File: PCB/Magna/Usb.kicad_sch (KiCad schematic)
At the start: 13 parts, among them J801 USB_A, J802 USB_C_Receptacle_USB2.0, U702 USB3300-EZK

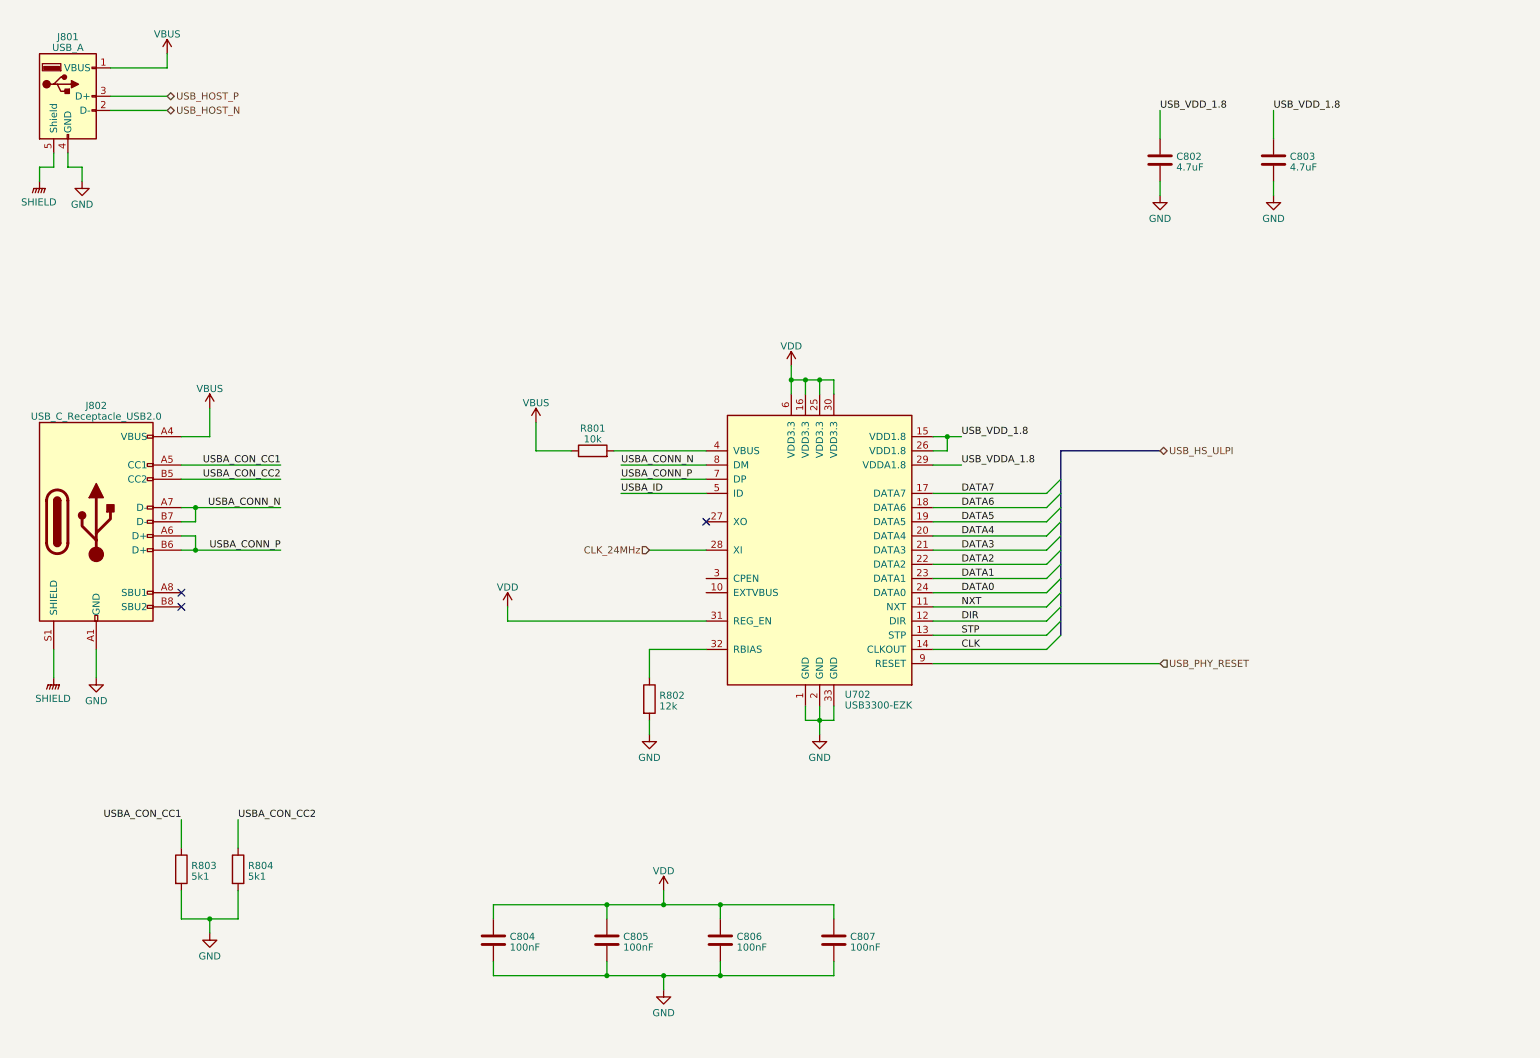
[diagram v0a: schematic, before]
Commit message: Update analogue frontend and add potentiometer interface
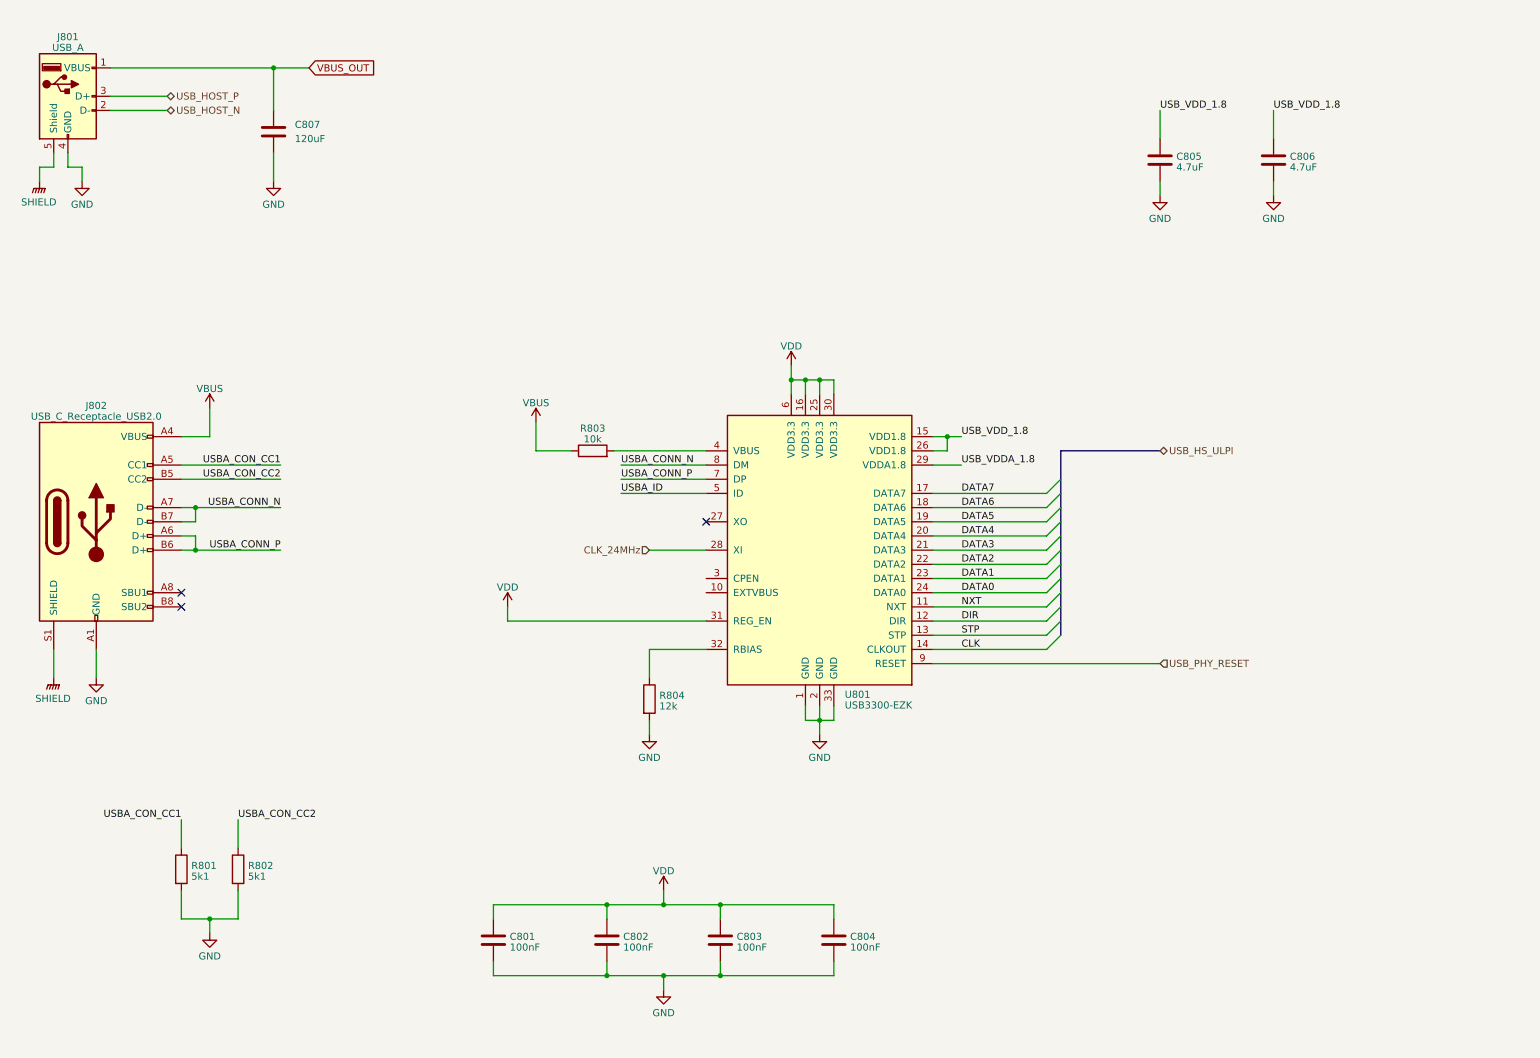
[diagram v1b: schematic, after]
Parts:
- added C807: 120uF, symbol Device:C
- renumbered C804 to C801, C805 to C802, C806 to C803, C807 to C804, C802 to C805, C803 to C806, R803 to R801, R804 to R802, R801 to R803, R802 to R804, U702 to U801
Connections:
- net GND: now also C807.2
- net VBUS: no longer J801.1 (VBUS)
- new net VBUS_OUT: C807.1, J801.1 (VBUS)

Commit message: Update USB schematic with ESD protection and extra port
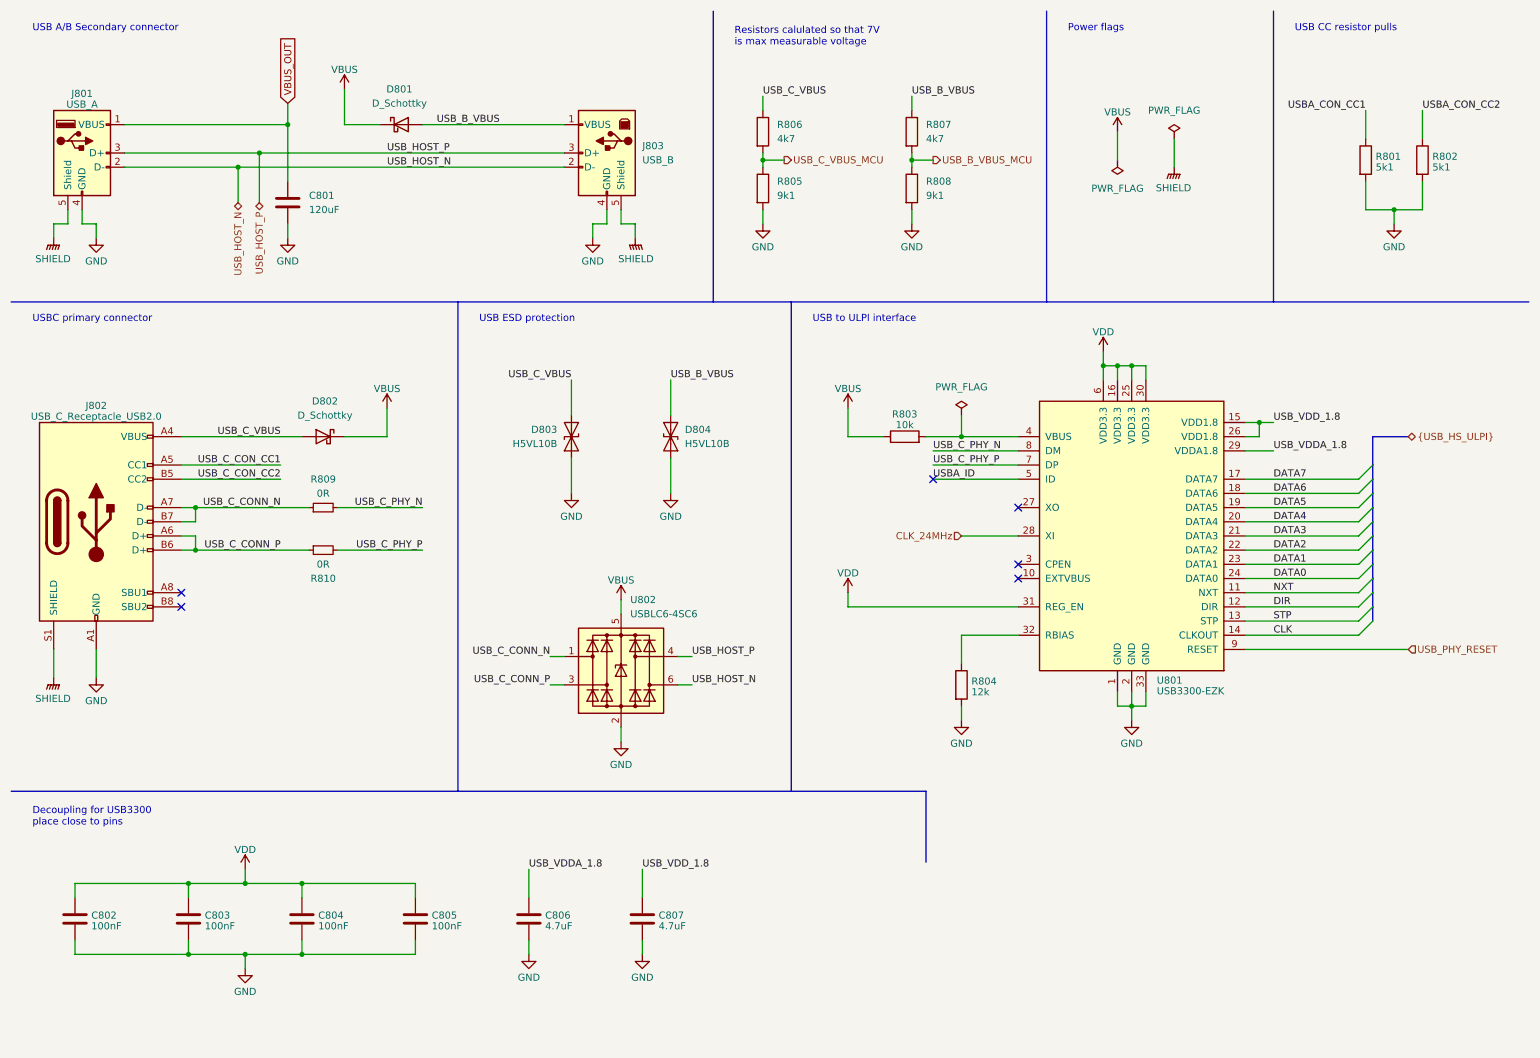
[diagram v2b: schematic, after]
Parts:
- added D801, D802: D_Schottky, symbol Device:D_Schottky
- added D803, D804: H5VL10B, symbol Diode:ESD9B5.0ST5G
- added J803: USB_B, symbol Connector:USB_B
- added R805, R808: 9k1, symbol Device:R
- added R806, R807: 4k7, symbol Device:R
- added R809, R810: 0R, symbol Device:R_Small
- added U802: USBLC6-4SC6, Package_TO_SOT_SMD:SOT-23-6, symbol Power_Protection:USBLC6-4SC6
- renumbered C807 to C801, C801 to C802, C802 to C803, C803 to C804, C804 to C805, C805 to C806, C806 to C807
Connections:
- net GND: now also D803.1 (A1), D804.1 (A1), J803.4 (GND), R805.2, R808.2, U802.2 (GND)
- net SHIELD: now also J803.5 (Shield)
- net USBA_CON_CC1: no longer J802.A5 (CC1)
- net USBA_CON_CC2: no longer J802.B5 (CC2)
- net USB_HOST_N: now also J803.2 (D-), U802.6 (I/O4)
- net USB_HOST_P: now also J803.3 (D+), U802.4 (I/O3)
- net USB_VDDA_1.8: now also C806.1
- net USB_VDD_1.8: no longer C806.1
- net VBUS: now also D801.1 (K), D802.1 (K), U802.5 (VBUS); no longer J802.A4 (VBUS), J802.A9 (VBUS), J802.B4 (VBUS), J802.B9 (VBUS)
- net USBA_CONN_N renamed USB_C_CONN_N
- net USB_C_CONN_N: now also R809.1, U802.1 (I/O1); no longer U801.8 (DM)
- net USBA_CONN_P renamed USB_C_CONN_P
- net USB_C_CONN_P: now also R810.1, U802.3 (I/O2); no longer U801.7 (DP)
- new net USB_B_VBUS: D801.2 (A), D804.2 (A2), J803.1 (VBUS), R807.1
- new net USB_B_VBUS_MCU: R807.2, R808.1
- new net USB_C_CON_CC1: J802.A5 (CC1)
- new net USB_C_CON_CC2: J802.B5 (CC2)
- new net USB_C_PHY_N: R809.2, U801.8 (DM)
- new net USB_C_PHY_P: R810.2, U801.7 (DP)
- new net USB_C_VBUS: D802.2 (A), D803.2 (A2), J802.A4 (VBUS), J802.A9 (VBUS), J802.B4 (VBUS), J802.B9 (VBUS), R806.1
- new net USB_C_VBUS_MCU: R805.1, R806.2
- no-connect marks 3 -> 6
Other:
- note added: "Decoupling for USB3300 place close to pins"
- note added: "Power flags"
- note added: "Resistors calulated so that 7V is max measurable voltage"
- note added: "USB A/B Secondary connector"
- note added: "USB CC resistor pulls"
- note added: "USB ESD protection"
- note added: "USB to ULPI interface"
- note added: "USBC primary connector"
- moved on the sheet: C801, C802, C803, C804, C805, C806, C807, J801, R801, R802, R803, R804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

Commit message: Remove all ERC in schematics
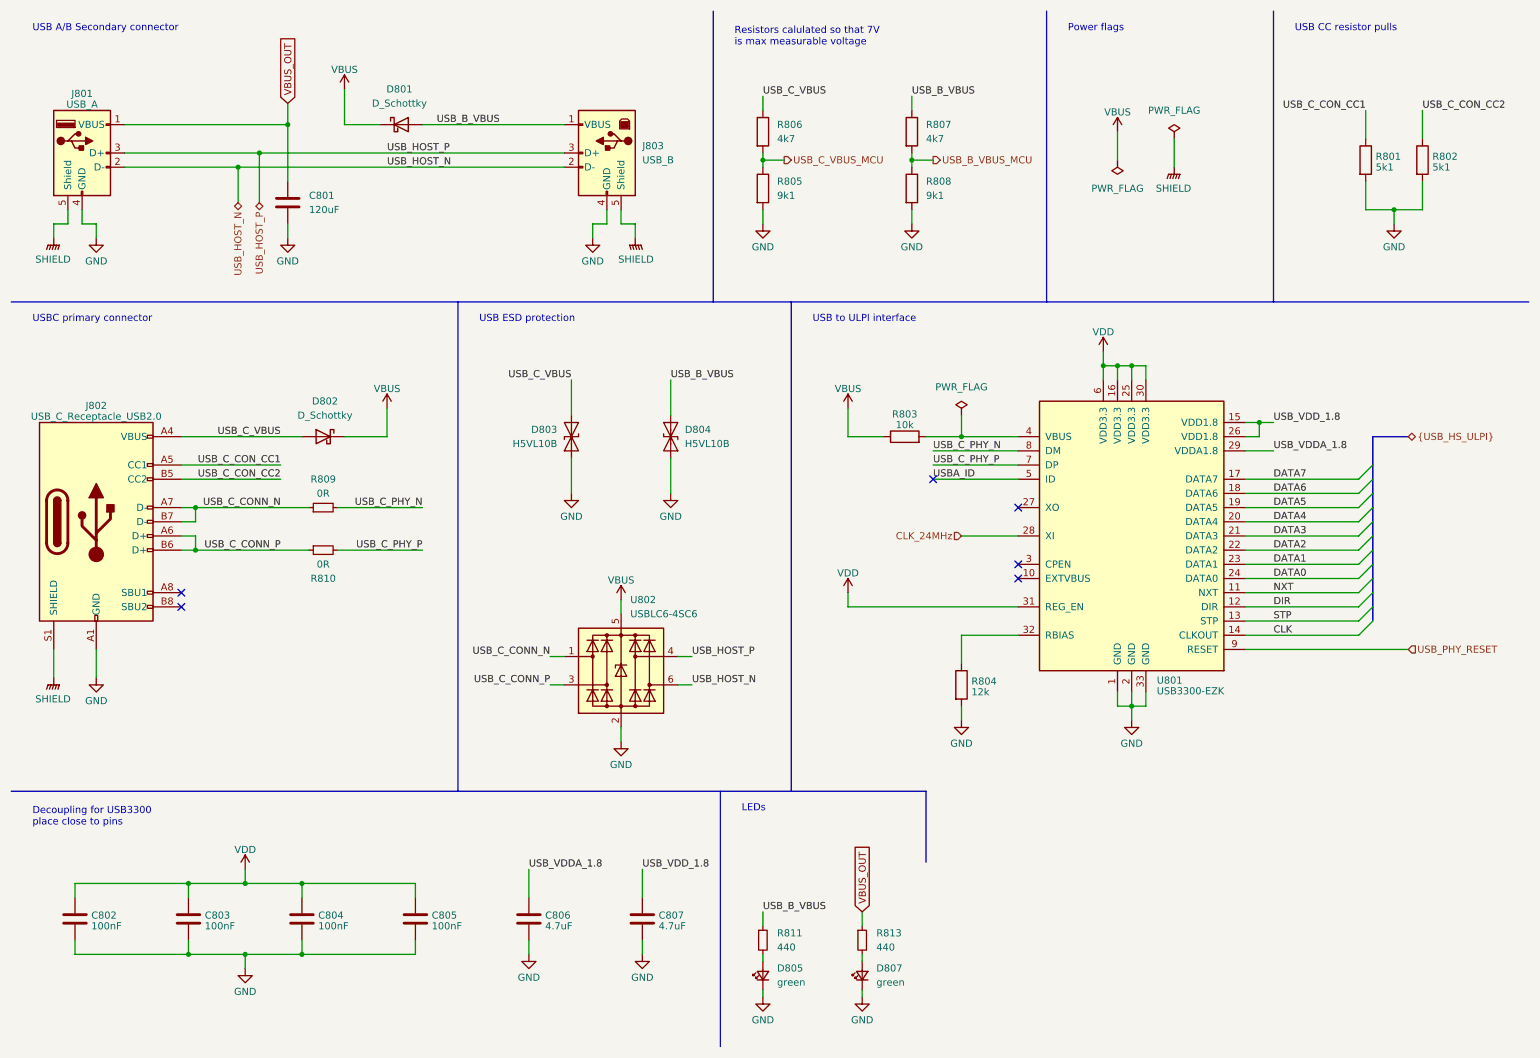
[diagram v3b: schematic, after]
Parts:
- added D805, D807: green, symbol Device:LED_Small
- added R811, R813: 440, symbol Device:R_Small
- J802: symbol Connector:USB_C_Receptacle_USB2.0 -> Connector:USB_C_Receptacle_USB2.0_16P
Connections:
- net USBA_CON_CC1 is gone; now on net USB_C_CON_CC1: R801.1
- net USBA_CON_CC2 is gone; now on net USB_C_CON_CC2: R802.1
- net GND: now also D805.1 (K), D807.1 (K)
- net USB_B_VBUS: now also R811.1
- net VBUS_OUT: now also R813.1
- new net: D805.2 (A), R811.2
- new net: D807.2 (A), R813.2
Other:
- note added: "LEDs"

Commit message: Update capacitors to parts in JLC library
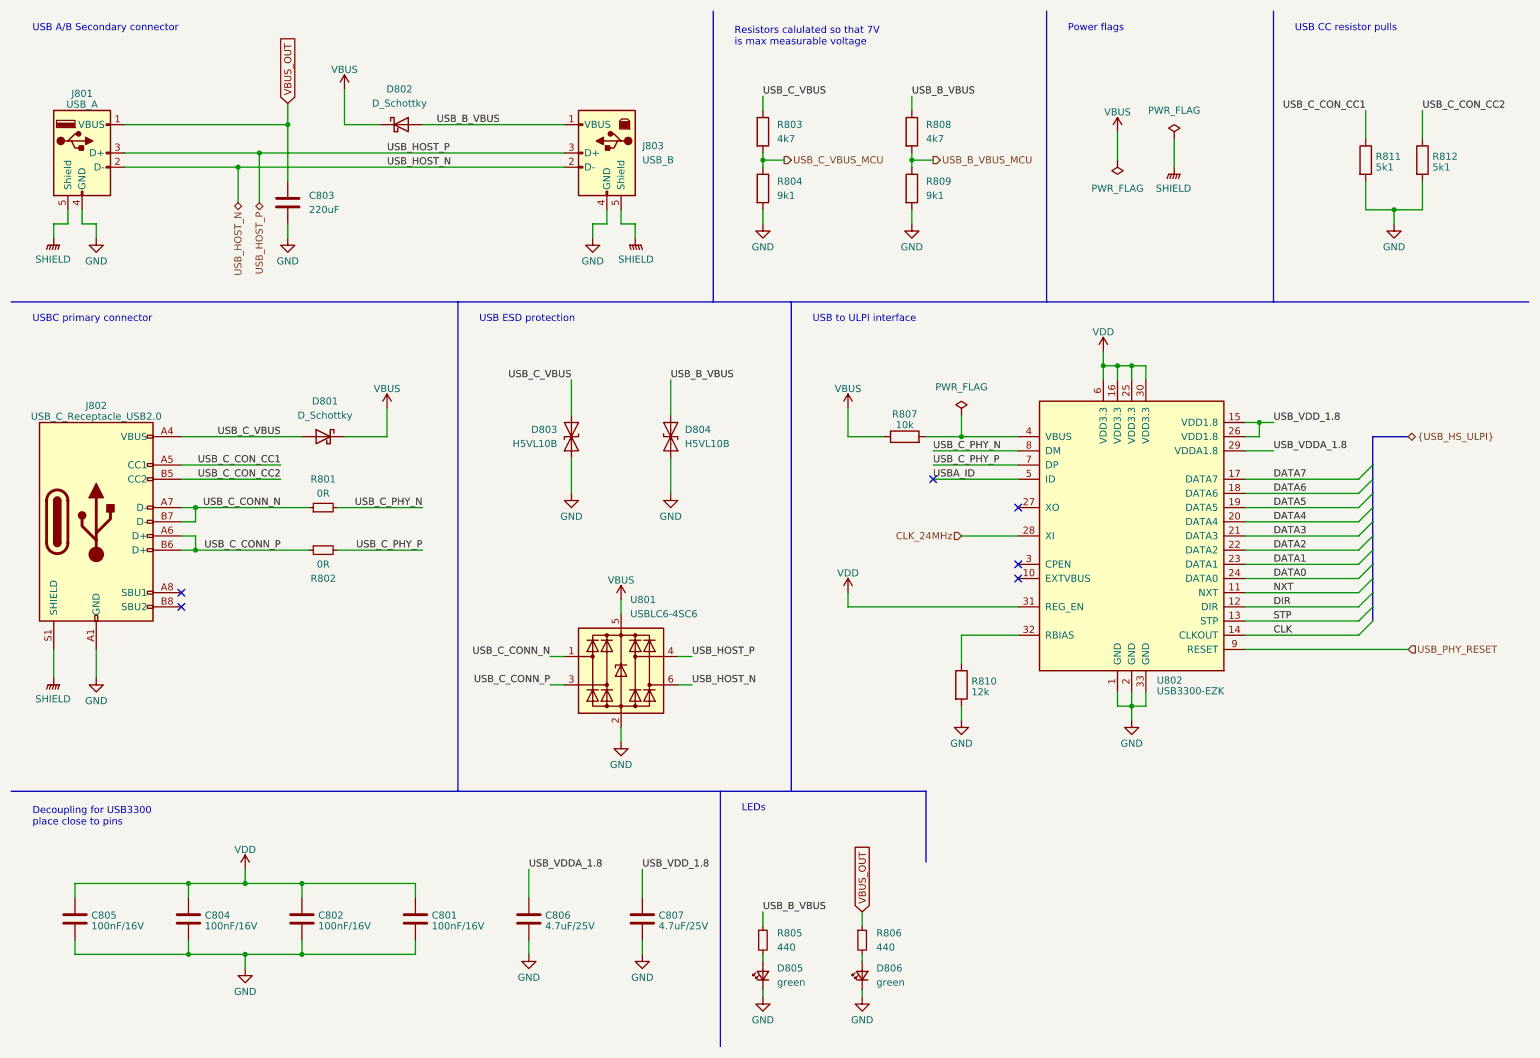
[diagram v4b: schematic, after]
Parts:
- removed C803: 100nF, Capacitor_SMD:C_0402_1005Metric, symbol Device:C
- added C801: 100nF/16V, Capacitor_SMD:C_0805_2012Metric, symbol Device:C
- C802, C804, C805: value 100nF -> 100nF/16V; footprint Capacitor_SMD:C_0402_1005Metric -> Capacitor_SMD:C_0805_2012Metric; LCSC C1525 -> C218638
- C803: renamed from C801; value 120uF -> 220uF; footprint (none) -> Capacitor_SMD:CP_Elec_4x5.8; LCSC (none) -> C2165067
- C806, C807: value 4.7uF -> 4.7uF/25V; footprint Capacitor_SMD:C_0402_1005Metric -> Capacitor_SMD:C_0805_2012Metric; LCSC C23733 -> C1779
- R811: renamed from R801; LCSC (none) -> C218638; LCSCL C17379 -> (none)
- R812: renamed from R802; LCSC (none) -> C218638; LCSCL C17379 -> (none)
- renumbered D802 to D801, D801 to D802, D807 to D806, R809 to R801, R810 to R802, R806 to R803, R805 to R804, R811 to R805, R813 to R806, R803 to R807, R807 to R808, R808 to R809, R804 to R810, U802 to U801, U801 to U802
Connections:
- net GND: now also C801.2
- net VDD: now also C801.1
